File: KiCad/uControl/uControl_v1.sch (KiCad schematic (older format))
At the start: 29 parts, among them IC1 ATMEGA328-PU, P13 AREF, P14 ANALOG_5V0, P15 ANALOG_GND, P4 PWM_SERVO, P5 5V_SERVO, P6 GND_SERVO, P8 FTDI, P9 ICSP, SW1 SW_PUSH, U2 74HC125, X1 CRYSTAL_2

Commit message: uControl schematic development. To Do decide on control pins for Pump, Pressure and Valve
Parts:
- removed C14: 100n, c_0805, symbol C
- removed R3, R4, R6: 10k, r_0805, symbol R
- removed SD1: SD_CARD_MICRO, SD_Micro, symbol SD_CARD_MICRO
- removed U2: 74HC125, SO14E, symbol 74LS125
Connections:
- net labels added: PD2, PD3, Pressure, Pump, Valve
- net labels removed: PD2_1pps, PD4_GPS_Rx, PD6_GPS_Tx, SD_CLK, SD_CS, SD_DATA_IN, SD_DATA_OUT
- wire segments 249 -> 200
- no-connect marks 11 -> 4
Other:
- note added: "TO DO :\nDecide which ports to choose for\n-> Pressure\n-> Pump\n-> Valve"
- note removed: "PD2 (1pps)\nGPS 1pps signal"
- note removed: "PD3 (SQW)\nRTC 1Hz signal"
- moved on the sheet: P14, P15, SHIELD1

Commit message: uControl schematic progress
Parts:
- removed C8: 47u,10V, C_ELCO_SMD, symbol C_POL
- removed D8: MBRM110LT1G, do_457, symbol DIODESCH
- removed F2: nanoSMDC110F, f_1206, symbol FUSE
- removed P4: PWM_SERVO, Header_Servo, symbol CONN_8
- removed P5: 5V_SERVO, Header_Servo, symbol CONN_8
- removed P6: GND_SERVO, Header_Servo, symbol CONN_8
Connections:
- net labels added: ~Flow_Tx, ~MOSI, ~PB1, ~PD3, ~SS, ~Valve
- net labels removed: 5V_INT, 5V_SERVO, Flow_Tx, MOSI, PB1, PC3, PD3, PD3_SQW, PD5, PD7, SS, Valve
- wire segments 200 -> 162
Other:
- note removed: "Connect ext. Servo supply to 5V_Servo and GND_SERVO Connectors,\nPins 7/8 or use jumper link between Pins 7/8 of \nPWM_SERVO and 5V_SERVO connectors when using on board 5V"
- note removed: "PWM1"
- note removed: "PWM2"
- note removed: "PWM3"
- note removed: "PWM4"
- note removed: "PWM5"
- note removed: "PWM6"
- note removed: "SERVO Header"
- note removed: "TO DO :\nDecide which ports to choose for\n-> Pressure\n-> Pump\n-> Valve"

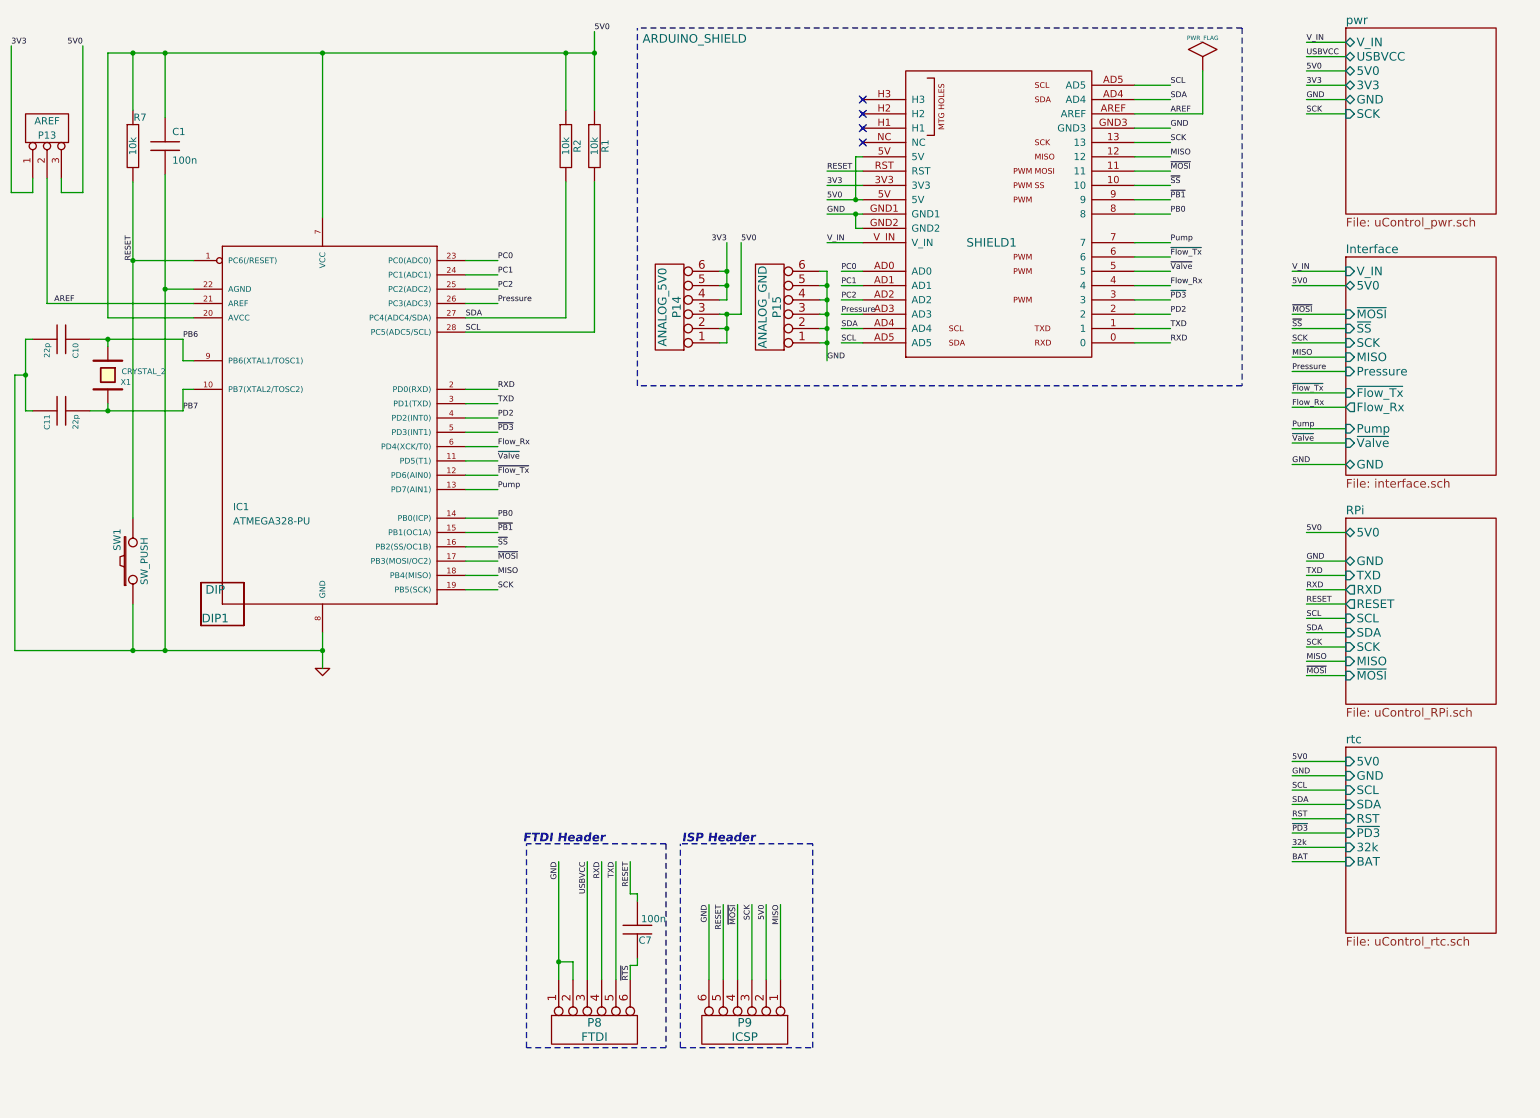
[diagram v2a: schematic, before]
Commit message: uControl schematic in progress
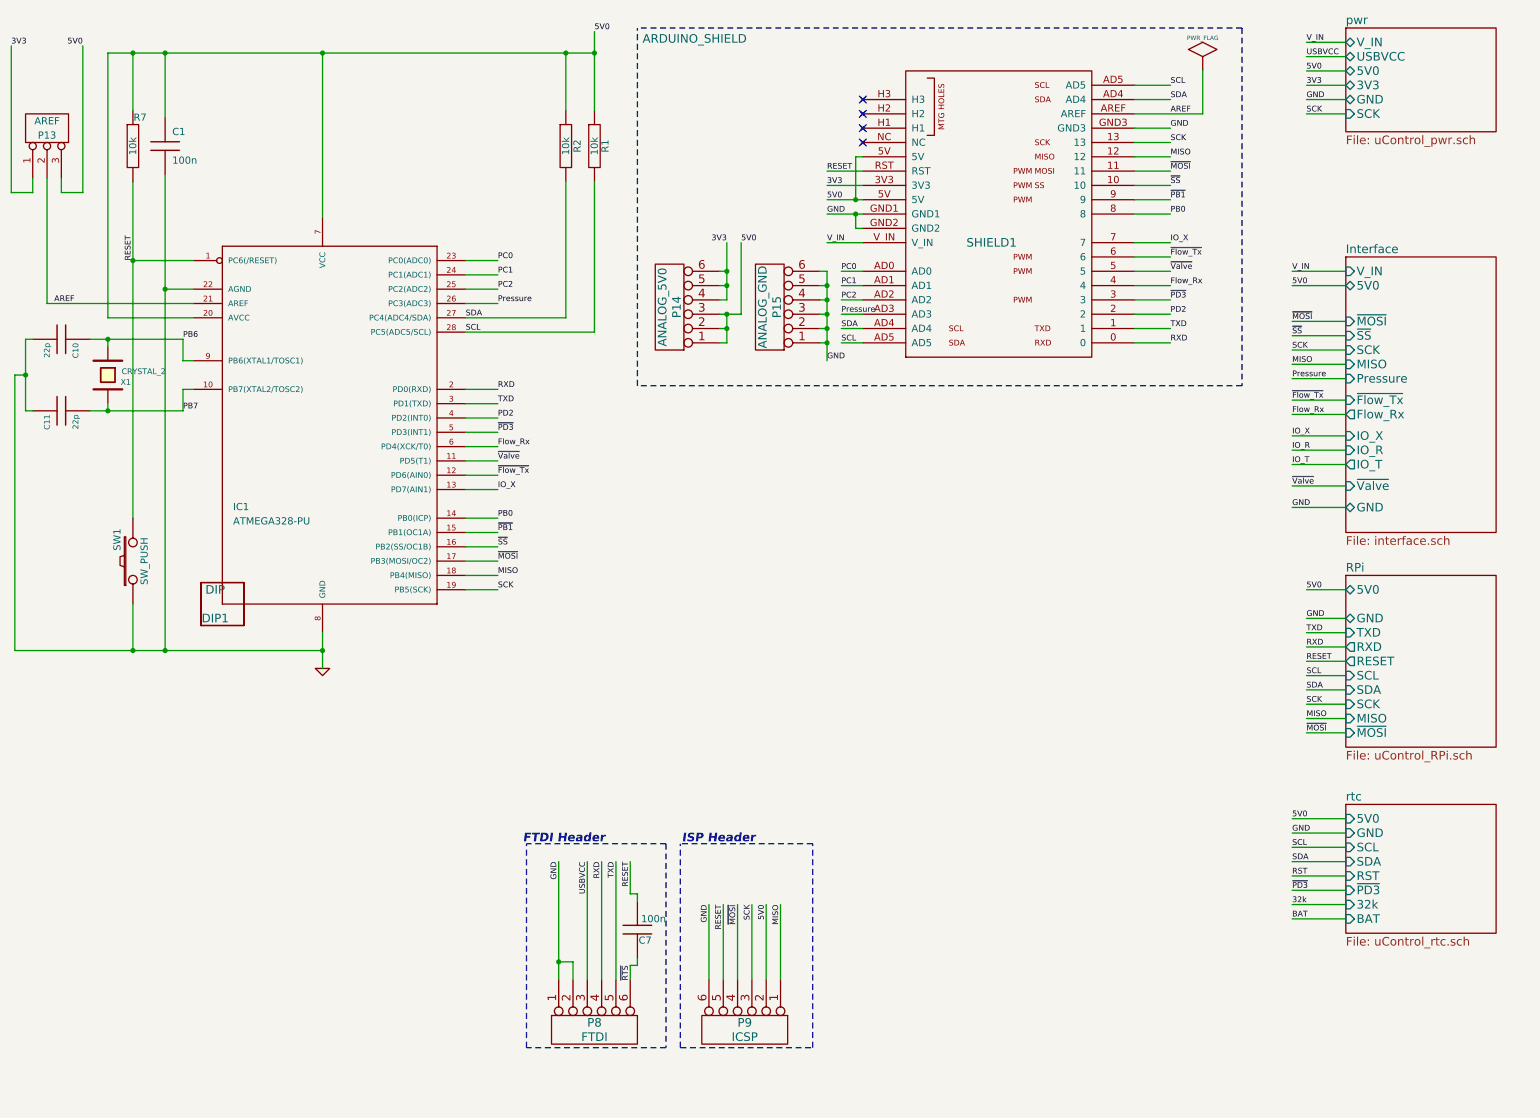
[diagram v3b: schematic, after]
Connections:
- net Pump renamed IO_X
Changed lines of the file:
@@
-EESchema Schematic File Version 2  date 11/29/2012 6:28:02 PM
+EESchema Schematic File Version 2  date 11/30/2012 11:17:28 AM
 LIBS:uControl
 LIBS:Conn-raspberry
@@
 Sheet 1 5
 Title "uControl"
-Date "29 nov 2012"
+Date "30 nov 2012"
 Rev "1"
 Comp "WyoLum"
@@
 Comment4 ""
 $EndDescr
-Wire Wire Line
-	9675 3525 10050 3525
-Wire Wire Line
-	9675 3275 10050 3275
-Wire Wire Line
-	9675 3025 10050 3025
-Wire Wire Line
-	9675 2825 10050 2825
-Wire Wire Line
-	9675 2625 10050 2625
+Text Label 9675 3675 0    40   ~ 0
+IO_T
+Text Label 9675 3575 0    40   ~ 0
+IO_R
+Wire Wire Line
+	9675 3675 10050 3675
+Wire Wire Line
+	9675 3825 10050 3825
+Wire Wire Line
+	9675 3325 10050 3325
+Wire Wire Line
+	9675 3075 10050 3075
+Wire Wire Line
+	9675 2875 10050 2875
+Wire Wire Line
+	9675 2675 10050 2675
 Wire Wire Line
 	9675 2325 10050 2325
@@
 	4650 7275 4650 7150
 Wire Wire Line
+	9775 5150 10050 5150
+Wire Wire Line
+	9775 4950 10050 4950
+Wire Wire Line
 	9775 4750 10050 4750
 Wire Wire Line
-	9775 4550 10050 4550
-Wire Wire Line
-	9775 4350 10050 4350
-Wire Wire Line
 	9775 1225 10050 1225
 Wire Wire Line
@@
 	6675 1725 6425 1725
 Wire Wire Line
-	9675 6450 10050 6450
-Wire Wire Line
-	9675 6350 10050 6350
-Wire Wire Line
-	9675 6150 10050 6150
+	9675 6850 10050 6850
+Wire Wire Line
+	9675 6750 10050 6750
+Wire Wire Line
+	9675 6550 10050 6550
 Wire Wire Line
 	1400 3250 1400 3300
@@
 	6675 2725 6525 2725
 Wire Wire Line
-	9675 6050 10050 6050
-Wire Wire Line
-	9675 5750 10050 5750
+	9675 6450 10050 6450
+Wire Wire Line
+	9675 6150 10050 6150
 Wire Wire Line
 	6425 1825 6675 1825
@@
 	6675 1925 6425 1925
 Wire Wire Line
-	9675 5950 10050 5950
-Wire Wire Line
-	9675 5850 10050 5850
+	9675 6350 10050 6350
+Wire Wire Line
+	9675 6250 10050 6250
 Wire Wire Line
 	6675 2825 6525 2825
@@
 	4125 2550 3900 2550
 Wire Wire Line
-	9675 6250 10050 6250
+	9675 6650 10050 6650
 Wire Wire Line
 	6625 1825 6625 1525
@@
 	9775 1125 10050 1125
 Wire Wire Line
-	9775 4450 10050 4450
-Wire Wire Line
-	9775 4650 10050 4650
+	9775 4850 10050 4850
+Wire Wire Line
+	9775 5050 10050 5050
 Wire Wire Line
 	9050 925  9050 1225
@@
 	9050 1225 8575 1225
 Wire Wire Line
-	9775 5050 10050 5050
-Wire Wire Line
-	9775 4850 10050 4850
-Wire Wire Line
-	9775 4950 10050 4950
-Wire Wire Line
-	9775 5150 10050 5150
-Wire Wire Line
-	9775 4150 10050 4150
+	9775 5450 10050 5450
+Wire Wire Line
+	9775 5250 10050 5250
+Wire Wire Line
+	9775 5350 10050 5350
+Wire Wire Line
+	9775 5550 10050 5550
+Wire Wire Line
+	9775 4550 10050 4550
 Wire Notes Line
 	5300 6325 4325 6325
@@
 	9675 2425 10050 2425
 Wire Wire Line
-	9675 2725 10050 2725
-Wire Wire Line
-	9675 2925 10050 2925
-Wire Wire Line
-	9675 3175 10050 3175
-Wire Wire Line
-	9675 3425 10050 3425
-Wire Wire Line
-	9675 3675 10050 3675
+	9675 2775 10050 2775
+Wire Wire Line
+	9675 2975 10050 2975
+Wire Wire Line
+	9675 3225 10050 3225
+Wire Wire Line
+	9675 3475 10050 3475
+Wire Wire Line
+	9675 3975 10050 3975
+Wire Wire Line
+	10050 3575 9675 3575
 Text Label 9675 2325 0    40   ~ 0
 V_IN
 Text Label 9675 2425 0    40   ~ 0
 5V0
-Text Label 9675 2625 0    40   ~ 0
+Text Label 9675 2675 0    40   ~ 0
 ~MOSI
-Text Label 9675 2725 0    40   ~ 0
+Text Label 9675 2775 0    40   ~ 0
 ~SS
-Text Label 9675 2825 0    40   ~ 0
+Text Label 9675 2875 0    40   ~ 0
 SCK
-Text Label 9675 2925 0    40   ~ 0
+Text Label 9675 2975 0    40   ~ 0
 MISO
-Text Label 9675 3025 0    40   ~ 0
+Text Label 9675 3075 0    40   ~ 0
 Pressure
-Text Label 9675 3175 0    40   ~ 0
+Text Label 9675 3225 0    40   ~ 0
 ~Flow_Tx
-Text Label 9675 3275 0    40   ~ 0
+Text Label 9675 3325 0    40   ~ 0
 Flow_Rx
-Text Label 9675 3425 0    40   ~ 0
-Pump
-Text Label 9675 3525 0    40   ~ 0
+Text Label 9675 3475 0    40   ~ 0
+IO_X
+Text Label 9675 3825 0    40   ~ 0
 ~Valve
-Text Label 9675 3675 0    40   ~ 0
+Text Label 9675 3975 0    40   ~ 0
 GND
 $Sheet
-S 10050 2225 1050 1525
+S 10050 2225 1050 1925
 U 50B2116F
 F0 "Interface" 60
 F1 "interface.sch" 60
-F2 "Pump" I L 10050 3425 60
-F3 "SCK" I L 10050 2825 60
-F4 "MISO" I L 10050 2925 60
-F5 "Pressure" I L 10050 3025 60
-F6 "V_IN" I L 10050 2325 60
-F7 "Flow_Rx" O L 10050 3275 60
-F8 "GND" B L 10050 3675 60
-F9 "5V0" B L 10050 2425 60
-F10 "~Valve" I L 10050 3525 60
-F11 "~Flow_Tx" I L 10050 3175 60
-F12 "~MOSI" I L 10050 2625 60
-F13 "~SS" I L 10050 2725 60
+F2 "SCK" I L 10050 2875 60
+F3 "MISO" I L 10050 2975 60
+F4 "Pressure" I L 10050 3075 60
+F5 "V_IN" I L 10050 2325 60
+F6 "Flow_Rx" O L 10050 3325 60
+F7 "GND" B L 10050 3975 60
+F8 "5V0" B L 10050 2425 60
+F9 "~Valve" I L 10050 3825 60
+F10 "~Flow_Tx" I L 10050 3225 60
+F11 "~MOSI" I L 10050 2675 60
+F12 "~SS" I L 10050 2775 60
+F13 "IO_T" O L 10050 3675 60
+F14 "IO_R" I L 10050 3575 60
+F15 "IO_X" I L 10050 3475 60
 $EndSheet
 Text Label 5825 2125 0    40   ~ 0
@@
 Text Label 5050 7175 3    40   ~ 0
 ~RTS
-Text Label 9775 4150 0    40   ~ 0
+Text Label 9775 4550 0    40   ~ 0
 5V0
-Text Label 9775 4850 0    40   ~ 0
+Text Label 9775 5250 0    40   ~ 0
 SDA
-Text Label 9775 4950 0    40   ~ 0
+Text Label 9775 5350 0    40   ~ 0
 SCK
-Text Label 9775 5050 0    40   ~ 0
+Text Label 9775 5450 0    40   ~ 0
 MISO
-Text Label 9775 5150 0    40   ~ 0
+Text Label 9775 5550 0    40   ~ 0
 ~MOSI
 $Comp
-L PWR_FLAG #FLG1
+L PWR_FLAG #FLG01
 U 1 1 4FC9DB7D
 P 9050 925
-F 0 "#FLG1" H 9050 1195 30  0001 C CNN
+F 0 "#FLG01" H 9050 1195 30  0001 C CNN
 F 1 "PWR_FLAG" H 9050 1155 30  0000 C CNN
 	1    9050 925
 	1    0    0    -1
 $EndComp
+Text Label 9775 5150 0    40   ~ 0
+SCL
+Text Label 9775 5050 0    40   ~ 0
+RESET
+Text Label 9775 4950 0    40   ~ 0
+RXD
+Text Label 9775 4850 0    40   ~ 0
+TXD
 Text Label 9775 4750 0    40   ~ 0
-SCL
-Text Label 9775 4650 0    40   ~ 0
-RESET
-Text Label 9775 4550 0    40   ~ 0
-RXD
-Text Label 9775 4450 0    40   ~ 0
-TXD
-Text Label 9775 4350 0    40   ~ 0
 GND
 Text Label 9775 1225 0    40   ~ 0
@@
 V_IN
 $Sheet
-S 10050 625  1050 1300
+S 10050 625  1050 725
 U 4FC07407
 F0 "pwr" 60
@@
 $EndComp
 $Sheet
-S 10050 5650 1050 1300
+S 10050 6050 1050 900
 U 4E1FEA4E
 F0 "rtc" 60
 F1 "uControl_rtc.sch" 60
-F2 "GND" I L 10050 5850 60
-F3 "SDA" I L 10050 6050 60
-F4 "SCL" I L 10050 5950 60
-F5 "5V0" I L 10050 5750 60
-F6 "RST" I L 10050 6150 60
-F7 "32k" I L 10050 6350 60
-F8 "BAT" I L 10050 6450 60
-F9 "~PD3" I L 10050 6250 60
+F2 "GND" I L 10050 6250 60
+F3 "SDA" I L 10050 6450 60
+F4 "SCL" I L 10050 6350 60
+F5 "5V0" I L 10050 6150 60
+F6 "RST" I L 10050 6550 60
+F7 "32k" I L 10050 6750 60
+F8 "BAT" I L 10050 6850 60
+F9 "~PD3" I L 10050 6650 60
 $EndSheet
 Text Label 8825 1825 0    40   ~ 0
@@
 PB0
 Text Label 8825 2125 0    40   ~ 0
-Pump
+IO_X
 Text Label 8825 2225 0    40   ~ 0
 ~Flow_Tx
@@
 V_IN
 $Sheet
-S 10050 4050 1050 1300
+S 10050 4450 1050 1200
 U 4FBF6CBF
 F0 "RPi" 60
 F1 "uControl_RPi.sch" 60
-F2 "GND" B L 10050 4350 60
-F3 "TXD" I L 10050 4450 60
-F4 "RXD" O L 10050 4550 60
-F5 "SCL" I L 10050 4750 60
-F6 "SDA" I L 10050 4850 60
-F7 "MISO" I L 10050 5050 60
-F8 "5V0" B L 10050 4150 60
-F9 "SCK" I L 10050 4950 60
-F10 "RESET" O L 10050 4650 60
-F11 "~MOSI" I L 10050 5150 60
+F2 "GND" B L 10050 4750 60
+F3 "TXD" I L 10050 4850 60
+F4 "RXD" O L 10050 4950 60
+F5 "SCL" I L 10050 5150 60
+F6 "SDA" I L 10050 5250 60
+F7 "MISO" I L 10050 5450 60
+F8 "5V0" B L 10050 4550 60
+F9 "SCK" I L 10050 5350 60
+F10 "RESET" O L 10050 5050 60
+F11 "~MOSI" I L 10050 5550 60
 $EndSheet
 Text Label 1925 3300 0    40   ~ 0
@@
 PB6
 $Comp
-L GND #PWR1
+L GND #PWR02
 U 1 1 4F5AFC62
 P 2900 5100
-F 0 "#PWR1" H 2900 5100 30  0001 C CNN
+F 0 "#PWR02" H 2900 5100 30  0001 C CNN
 F 1 "GND" H 2900 5030 30  0001 C CNN
 	1    2900 5100
@@
 Text Label 6425 1725 0    40   ~ 0
 3V3
-Text Label 9675 6450 0    40   ~ 0
+Text Label 9675 6850 0    40   ~ 0
 BAT
-Text Label 9675 6350 0    40   ~ 0
+Text Label 9675 6750 0    40   ~ 0
 32k
-Text Label 9675 6250 0    40   ~ 0
+Text Label 9675 6650 0    40   ~ 0
 ~PD3
-Text Label 9675 6150 0    40   ~ 0
+Text Label 9675 6550 0    40   ~ 0
 RST
 $Comp
@@
 Text Label 6525 2725 0    40   ~ 0
 SDA
-Text Label 9675 5850 0    40   ~ 0
+Text Label 9675 6250 0    40   ~ 0
 GND
-Text Label 9675 6050 0    40   ~ 0
+Text Label 9675 6450 0    40   ~ 0
 SDA
-Text Label 9675 5950 0    40   ~ 0
+Text Label 9675 6350 0    40   ~ 0
 SCL
-Text Label 9675 5750 0    40   ~ 0
+Text Label 9675 6150 0    40   ~ 0
 5V0
 Text Label 6425 1925 0    40   ~ 0
@@
 PD2
 Text Label 4125 3850 0    40   ~ 0
-Pump
+IO_X
 Text Label 4125 3550 0    40   ~ 0
 Flow_Rx
